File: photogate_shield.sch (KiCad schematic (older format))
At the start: 16 parts, among them P1 CONN_6, P2 CONN_6, SW1 SW_PUSH

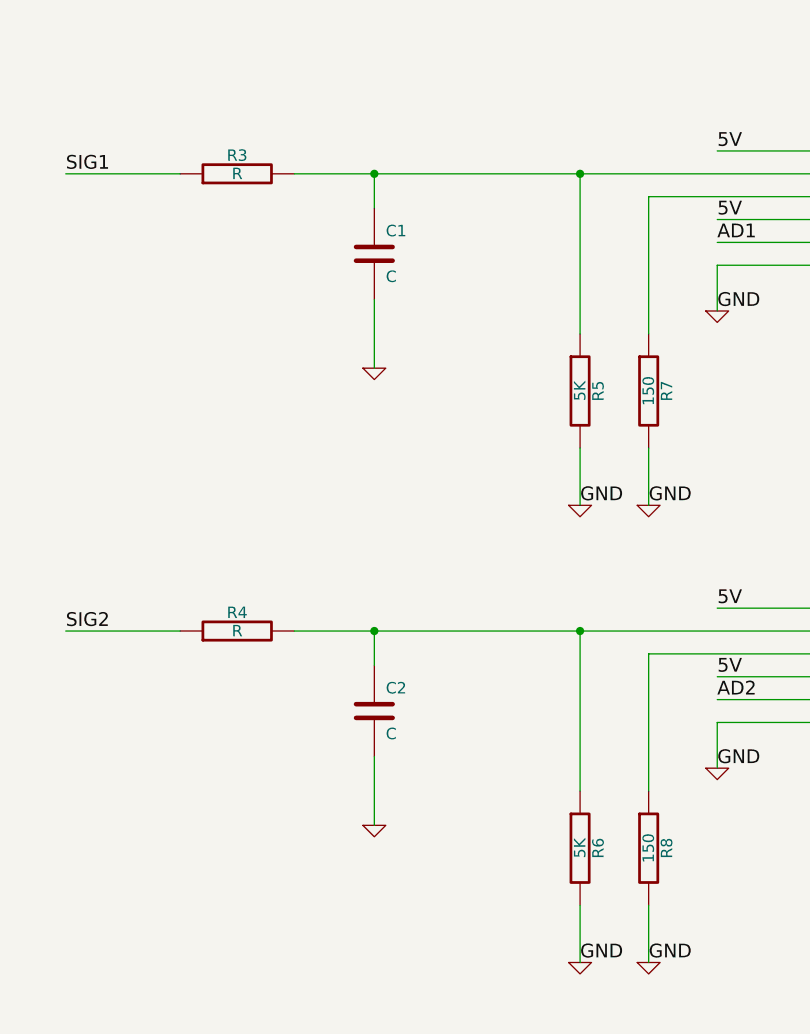
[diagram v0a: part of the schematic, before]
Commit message: Changed resistor value for phototransistor - gives better margin.
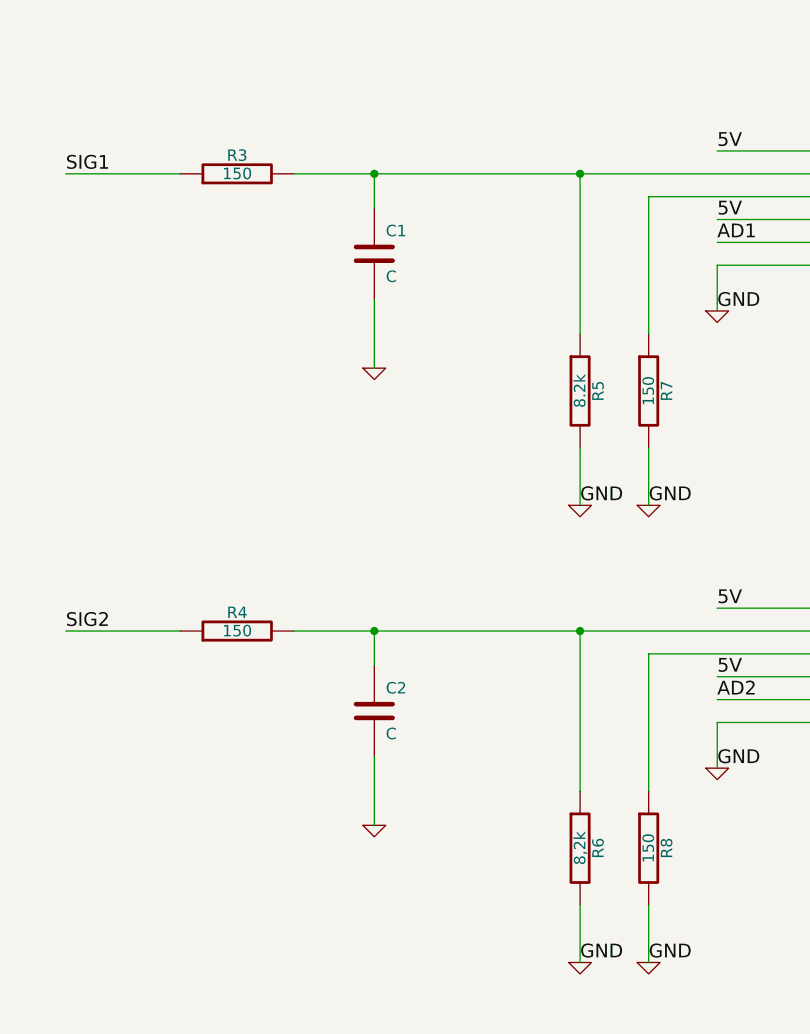
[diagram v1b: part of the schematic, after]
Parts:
- R3, R4: value R -> 150
- R5: value 5K -> 8.2k
- R6: value 5K -> 8,2k
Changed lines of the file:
@@
-EESchema Schematic File Version 2  date Thu 10 Jul 2014 06:34:42 PM PDT
+EESchema Schematic File Version 2
 LIBS:power
 LIBS:device
@@
 LIBS:arduino_shieldsNCL
 LIBS:photogate_shield-cache
-EELAYER 25  0
+EELAYER 27 0
 EELAYER END
-$Descr A4 11700 8267
+$Descr A4 11693 8268
 encoding utf-8
 Sheet 1 1
 Title ""
-Date "10 jul 2014"
+Date "14 apr 2015"
 Rev ""
 Comp ""
@@
 F 0 "#FLG01" H 650 895 30  0001 C CNN
 F 1 "PWR_FLAG" H 650 980 30  0000 C CNN
+F 2 "" H 650 800 60  0001 C CNN
+F 3 "" H 650 800 60  0001 C CNN
 	1    650  800
 	1    0    0    -1
@@
 F 0 "#FLG02" H 1250 895 30  0001 C CNN
 F 1 "PWR_FLAG" H 1250 980 30  0000 C CNN
+F 2 "" H 1250 800 60  0001 C CNN
+F 3 "" H 1250 800 60  0001 C CNN
 	1    1250 800
 	1    0    0    -1
@@
 F 0 "#PWR03" H 1250 1050 30  0001 C CNN
 F 1 "GND" H 1250 980 30  0001 C CNN
+F 2 "" H 1250 1050 60  0001 C CNN
+F 3 "" H 1250 1050 60  0001 C CNN
 	1    1250 1050
 	1    0    0    -1
@@
 F 0 "C2" H 8100 4100 50  0000 L CNN
 F 1 "C" H 8100 3900 50  0000 L CNN
+F 2 "" H 8050 4000 60  0001 C CNN
+F 3 "" H 8050 4000 60  0001 C CNN
 	1    8050 4000
 	1    0    0    -1
@@
 P 7450 3650
 F 0 "R4" V 7530 3650 50  0000 C CNN
-F 1 "R" V 7450 3650 50  0000 C CNN
+F 1 "150" V 7450 3650 50  0000 C CNN
+F 2 "" H 7450 3650 60  0001 C CNN
+F 3 "" H 7450 3650 60  0001 C CNN
 	1    7450 3650
 	0    -1   -1   0
@@
 F 0 "#PWR04" H 8050 4500 30  0001 C CNN
 F 1 "GND" H 8050 4430 30  0001 C CNN
+F 2 "" H 8050 4500 60  0001 C CNN
+F 3 "" H 8050 4500 60  0001 C CNN
 	1    8050 4500
 	1    0    0    -1
@@
 F 0 "#PWR05" H 8050 2500 30  0001 C CNN
 F 1 "GND" H 8050 2430 30  0001 C CNN
+F 2 "" H 8050 2500 60  0001 C CNN
+F 3 "" H 8050 2500 60  0001 C CNN
 	1    8050 2500
 	1    0    0    -1
@@
 P 7450 1650
 F 0 "R3" V 7530 1650 50  0000 C CNN
-F 1 "R" V 7450 1650 50  0000 C CNN
+F 1 "150" V 7450 1650 50  0000 C CNN
+F 2 "" H 7450 1650 60  0001 C CNN
+F 3 "" H 7450 1650 60  0001 C CNN
 	1    7450 1650
 	0    -1   -1   0
@@
 F 0 "C1" H 8100 2100 50  0000 L CNN
 F 1 "C" H 8100 1900 50  0000 L CNN
+F 2 "" H 8050 2000 60  0001 C CNN
+F 3 "" H 8050 2000 60  0001 C CNN
 	1    8050 2000
 	1    0    0    -1
@@
 F 0 "#PWR06" H 2450 5400 30  0001 C CNN
 F 1 "GND" H 2450 5330 30  0001 C CNN
+F 2 "" H 2450 5400 60  0001 C CNN
+F 3 "" H 2450 5400 60  0001 C CNN
 	1    2450 5400
 	1    0    0    -1
@@
 F 0 "SW1" H 2600 4760 50  0000 C CNN
 F 1 "SW_PUSH" H 2450 4570 50  0000 C CNN
+F 2 "" H 2450 4650 60  0001 C CNN
+F 3 "" H 2450 4650 60  0001 C CNN
 	1    2450 4650
 	0    -1   -1   0
@@
 F 0 "#PWR07" H 9550 2250 30  0001 C CNN
 F 1 "GND" H 9550 2180 30  0001 C CNN
+F 2 "" H 9550 2250 60  0001 C CNN
+F 3 "" H 9550 2250 60  0001 C CNN
 	1    9550 2250
 	1    0    0    -1
@@
 F 0 "#PWR08" H 9550 4250 30  0001 C CNN
 F 1 "GND" H 9550 4180 30  0001 C CNN
+F 2 "" H 9550 4250 60  0001 C CNN
+F 3 "" H 9550 4250 60  0001 C CNN
 	1    9550 4250
 	1    0    0    -1
@@
 F 0 "SHIELD1" H 3150 2950 60  0000 C CNN
 F 1 "ARDUINO_SHIELD" H 3550 1050 60  0000 C CNN
+F 2 "" H 3500 2000 60  0001 C CNN
+F 3 "" H 3500 2000 60  0001 C CNN
 	1    3500 2000
 	1    0    0    -1
@@
 P 8950 4600
 F 0 "R6" V 9030 4600 50  0000 C CNN
-F 1 "5K" V 8950 4600 50  0000 C CNN
+F 1 "8,2k" V 8950 4600 50  0000 C CNN
+F 2 "" H 8950 4600 60  0001 C CNN
+F 3 "" H 8950 4600 60  0001 C CNN
 	1    8950 4600
 	1    0    0    -1
@@
 F 0 "R8" V 9330 4600 50  0000 C CNN
 F 1 "150" V 9250 4600 50  0000 C CNN
+F 2 "" H 9250 4600 60  0001 C CNN
+F 3 "" H 9250 4600 60  0001 C CNN
 	1    9250 4600
 	1    0    0    -1
@@
 F 0 "#PWR09" H 9250 5100 30  0001 C CNN
 F 1 "GND" H 9250 5030 30  0001 C CNN
+F 2 "" H 9250 5100 60  0001 C CNN
+F 3 "" H 9250 5100 60  0001 C CNN
 	1    9250 5100
 	1    0    0    -1
@@
 F 0 "#PWR010" H 8950 5100 30  0001 C CNN
 F 1 "GND" H 8950 5030 30  0001 C CNN
+F 2 "" H 8950 5100 60  0001 C CNN
+F 3 "" H 8950 5100 60  0001 C CNN
 	1    8950 5100
 	1    0    0    -1
@@
 F 0 "P2" V 10350 3800 60  0000 C CNN
 F 1 "CONN_6" V 10450 3800 60  0000 C CNN
+F 2 "" H 10400 3800 60  0001 C CNN
+F 3 "" H 10400 3800 60  0001 C CNN
 	1    10400 3800
 	1    0    0    -1
@@
 F 0 "P1" V 10350 1800 60  0000 C CNN
 F 1 "CONN_6" V 10450 1800 60  0000 C CNN
+F 2 "" H 10400 1800 60  0001 C CNN
+F 3 "" H 10400 1800 60  0001 C CNN
 	1    10400 1800
 	1    0    0    -1
@@
 F 0 "R2" V 5430 4400 50  0000 C CNN
 F 1 "220" V 5350 4400 50  0000 C CNN
+F 2 "" H 5350 4400 60  0001 C CNN
+F 3 "" H 5350 4400 60  0001 C CNN
 	1    5350 4400
 	1    0    0    -1
@@
 F 0 "D2" H 5350 5150 50  0000 C CNN
 F 1 "LED" H 5350 4950 50  0000 C CNN
+F 2 "" H 5350 5050 60  0001 C CNN
+F 3 "" H 5350 5050 60  0001 C CNN
 	1    5350 5050
 	0    1    1    0
@@
 F 0 "#PWR011" H 5350 5400 30  0001 C CNN
 F 1 "GND" H 5350 5330 30  0001 C CNN
+F 2 "" H 5350 5400 60  0001 C CNN
+F 3 "" H 5350 5400 60  0001 C CNN
 	1    5350 5400
 	1    0    0    -1
@@
 F 0 "#PWR012" H 4850 5400 30  0001 C CNN
 F 1 "GND" H 4850 5330 30  0001 C CNN
+F 2 "" H 4850 5400 60  0001 C CNN
+F 3 "" H 4850 5400 60  0001 C CNN
 	1    4850 5400
 	1    0    0    -1
@@
 F 0 "#PWR013" H 8950 3100 30  0001 C CNN
 F 1 "GND" H 8950 3030 30  0001 C CNN
+F 2 "" H 8950 3100 60  0001 C CNN
+F 3 "" H 8950 3100 60  0001 C CNN
 	1    8950 3100
 	1    0    0    -1
@@
 F 0 "#PWR014" H 9250 3100 30  0001 C CNN
 F 1 "GND" H 9250 3030 30  0001 C CNN
+F 2 "" H 9250 3100 60  0001 C CNN
+F 3 "" H 9250 3100 60  0001 C CNN
 	1    9250 3100
 	1    0    0    -1
@@
 F 0 "D1" H 4850 5150 50  0000 C CNN
 F 1 "LED" H 4850 4950 50  0000 C CNN
+F 2 "" H 4850 5050 60  0001 C CNN
+F 3 "" H 4850 5050 60  0001 C CNN
 	1    4850 5050
 	0    1    1    0
@@
 F 0 "R1" V 4930 4400 50  0000 C CNN
 F 1 "220" V 4850 4400 50  0000 C CNN
+F 2 "" H 4850 4400 60  0001 C CNN
+F 3 "" H 4850 4400 60  0001 C CNN
 	1    4850 4400
 	1    0    0    -1
@@
 F 0 "R7" V 9330 2600 50  0000 C CNN
 F 1 "150" V 9250 2600 50  0000 C CNN
+F 2 "" H 9250 2600 60  0001 C CNN
+F 3 "" H 9250 2600 60  0001 C CNN
 	1    9250 2600
 	1    0    0    -1
@@
 P 8950 2600
 F 0 "R5" V 9030 2600 50  0000 C CNN
-F 1 "5K" V 8950 2600 50  0000 C CNN
+F 1 "8.2k" V 8950 2600 50  0000 C CNN
+F 2 "" H 8950 2600 60  0001 C CNN
+F 3 "" H 8950 2600 60  0001 C CNN
 	1    8950 2600
 	1    0    0    -1
